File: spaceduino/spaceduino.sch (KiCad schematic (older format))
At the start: 68 parts

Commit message: sntuff
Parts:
- removed Y?: XTAL, symbol Device:Crystal_GND2
- added C17, C18: 22pF, Capacitor_SMD:C_0603_1608Metric, symbol Device:C
- added H1, H2, H3, H4: MountingHole_Pad, MountingHole:MountingHole_2.7mm_Pad, symbol Mechanical:MountingHole_Pad
- added Y1: Crystal, Crystal:Crystal_HC49-U_Vertical, symbol Device:Crystal
- C1, C10, C11, C2, C3, C5, C6, C7, C9: renamed from C?; footprint (none) -> Capacitor_SMD:C_0603_1608Metric
- C12, C15, C16, C4, C8: renamed from C?; footprint (none) -> Capacitor_SMD:C_1206_3216Metric
- C13: renamed from C?; value C -> 1.5nF; footprint (none) -> Capacitor_SMD:C_0603_1608Metric
- C14: renamed from C?; value 100nF -> .1uF; footprint (none) -> Capacitor_SMD:C_0603_1608Metric
- D1, D2: renamed from D?; footprint (none) -> Diode_SMD:D_SOD-123
- D3, D4, D5, D6, D7: renamed from D?; footprint (none) -> LED_SMD:LED_1206_3216Metric
- F1: renamed from F?; footprint (none) -> Fuse:Fuse_1206_3216Metric
- J2: renamed from J?; footprint (none) -> Connector_Card:microSD_HC_Hirose_DM3D-SF
- J3: renamed from J?; footprint (none) -> Connector_PinHeader_2.54mm:PinHeader_2x03_P2.54mm_Vertical
- JCONTAINMENT1: renamed from JCONTAINMENT; footprint (none) -> Connector_PinHeader_2.54mm:PinHeader_1x12_P2.54mm_Vertical
- L1, L2: renamed from L?; footprint (none) -> Inductor_SMD:L_1210_3225Metric
- R1, R10, R11, R12, R13, R14, R15, R16, R17, R18, R19, R2, R20, R21, R22, R23, R24, R25, R26, R27, R3, R4, R5, R6, R7, R8, R9: renamed from R?; footprint (none) -> Resistor_SMD:R_1206_3216Metric
- SW1: renamed from SW?; footprint (none) -> Connector_PinHeader_2.54mm:PinHeader_1x02_P2.54mm_Vertical
- U6: renamed from U?; footprint (none) -> Package_SO:SOIC-8_3.9x4.9mm_P1.27mm
- gave numbers to parts that had none: 8
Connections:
- net +3V3 is gone; now on net +3V0: J2.4 (VDD)
- net I2C_SCL is gone; now on net i2c_scl: JCONTAINMENT1.5 (Pin_5)
- net I2C_SDA is gone; now on net i2c_sda: JCONTAINMENT1.4 (Pin_4)
- net GND: now also C17.2, C18.2, H1.1, H2.1, H3.1, H4.1
- net at U5.7 (XTAL2): now also C18.1, Y1.2
- net at U5.8 (XTAL1): now also C17.1, Y1.1
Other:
- note added: "mounting holes"

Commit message: something
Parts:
- removed C16: C, Capacitor_SMD:C_1206_3216Metric, symbol Device:C
- removed C9: .1uF, Capacitor_SMD:C_0603_1608Metric, symbol Device:C
- removed D2: D, Diode_SMD:D_SOD-123, symbol Device:D
- removed JCONTAINMENT1: Conn_01x12, Connector_PinHeader_2.54mm:PinHeader_1x12_P2.54mm_Vertical, symbol Connector_Generic:Conn_01x12
- removed R11: 5.6k, Resistor_SMD:R_1206_3216Metric, symbol Device:R
- removed R12: 13k, Resistor_SMD:R_1206_3216Metric, symbol Device:R
- removed R13, R16, R18, R26, R27, R9: R, Resistor_SMD:R_1206_3216Metric, symbol Device:R
- removed R14, R15: 1k, Resistor_SMD:R_1206_3216Metric, symbol Device:R
- removed U6: LM358, Package_SO:SOIC-8_3.9x4.9mm_P1.27mm, symbol Amplifier_Operational:LM358
- added C18: 10uF, Capacitor_SMD:C_0603_1608Metric, symbol Device:C
- added D1: D, Diode_SMD:D_SOD-123, symbol Device:D
- added FB1: Ferrite_Bead, Inductor_SMD:L_1206_3216Metric, symbol Device:Ferrite_Bead
- added J?: Conn_02x05_Odd_Even, symbol Connector_Generic:Conn_02x05_Odd_Even
- added LOGO1: Logo_Open_Hardware_Small, Spaceduino:spaceduino-logo, symbol Graphic:Logo_Open_Hardware_Small
- added Q?: PZT3904, Package_TO_SOT_SMD:SOT-223-3_TabPin2, symbol Transistor_BJT:PZT3904
- added R10: 10k, Resistor_SMD:R_1206_3216Metric, symbol Device:R
- added R6: 50m, Resistor_SMD:R_1206_3216Metric, symbol Device:R
- added U5, U7: INA226, Package_SO:VSSOP-10_3x3mm_P0.5mm, symbol Analog_ADC:INA226
- R11: renamed from R10; value .05 -> 50m
- R17: value R -> 10k
- R19, R20: value R -> 470
- R5: value .1 -> 10k
- SW1: footprint Connector_PinHeader_2.54mm:PinHeader_1x02_P2.54mm_Vertical -> Jumper:SolderJumper-2_P1.3mm_Open_TrianglePad1.0x1.5mm
- renumbered C17 to C11, C11 to C12, C18 to C13, C12 to C14, C13 to C15, C14 to C16, C15 to C17, D1 to D2, D4 to D3PWR1, D7 to DALERT1, D5 to DBPWR1, D6 to DIND1, D3 to DPWR1, R3 to R1, R21 to R12, R22 to R13, R23 to R14, R24 to R15, R25 to R16, R4 to R2, R1 to R3, R2 to R4, R6 to R7, R7 to R8, R8 to R9, U5 to U6
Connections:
- net current_trip is gone; now on net +5V: R16.1
- net sd_ss is gone; now on net 4_sd_ss: U3.10 (B4)
- net +5V: now also R17.1, R5.1, D1.1 (K), R10.1, U5.1 (A1), U5.2 (A0), U5.6 (VS), U7.6 (VS), U7.9 (Vin-)
- net 13: no longer R15.1
- net 3: now also R15.1
- net GND: now also C18.2, J?.9 (Pin_9), Q?.3 (E), U5.7 (GND), U7.1 (A1), U7.2 (A0), U7.7 (GND); no longer DALERT1.1 (K), R20.1
- net VDDF: now also R6.1, U5.9 (Vin-); no longer R5.1
- net a7: no longer R17.1
- net i2c_scl: now also J?.3 (Pin_3), U5.5 (SCL), U7.5 (SCL)
- net i2c_sda: now also J?.1 (Pin_1), U5.4 (SDA), U7.4 (SDA)
- net vusb: now also FB1.1; no longer F1.2
- net ~reset: now also R19.2, R5.2, D1.2 (A); no longer SW1.1 (A)
- net d-: now reaches C7.1, J1.2 (D-), R4.2
- net d+: now reaches C6.1, J1.3 (D+), R3.2
- net at Q1.3 (D): now also J?.5 (Pin_5)
- net at Q2.3 (D): now also J?.7 (Pin_7)
- net at C17.1, F1.1, R11.2: now also U7.10 (Vin+), U7.8 (Vbus); no longer R19.2
- net at C14.1, C15.1, D2.1 (K)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: now also R6.2, U5.10 (Vin+), U5.8 (Vbus); no longer R5.2
- net at R17.2: now also R20.1, C18.1, Q?.1 (B)
- net at R19.1: now also SW1.1 (A); no longer R20.2
- net at Q1.1 (G), Q2.1 (G): now also Q?.2 (C), Q?.4 (C), R10.2
- net 4 renamed 4_sd_ss
- new net: F1.2, FB1.2
- new net current_trip_fast: DALERT1.1 (K), R20.2, U7.3 (~Alert~)
- no-connect marks 9 -> 10
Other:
- note added: "<- can be LED"
- note added: "current limiting"
- note removed: "TODO: sense"
- note removed: "Voltage Monitoring"
- note removed: "circular connector"
- note removed: "increase ratio for\nlarge boost voltage"
- moved on the sheet: D3PWR1, DALERT1, DBPWR1, DIND1, DPWR1, H1, H2, H3, H4, Q1, Q2, R12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

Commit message: spaceduino simple finished
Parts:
- removed Q?: PZT3904, Package_TO_SOT_SMD:SOT-223-3_TabPin2, symbol Transistor_BJT:PZT3904
- added C19, C9: .1uF, Capacitor_SMD:C_0603_1608Metric, symbol Device:C
- added Q3: 2N7002, Package_TO_SOT_SMD:SOT-23, symbol Transistor_FET:2N7002
- added R18: 3.3k, Resistor_SMD:R_1206_3216Metric, symbol Device:R
- H1, H2, H3, H4: footprint MountingHole:MountingHole_2.7mm_Pad -> MountingHole:MountingHole_2.2mm_M2_Pad
- J4: renamed from J?; footprint (none) -> Connector_PinHeader_2.54mm:PinHeader_2x05_P2.54mm_Vertical
- R10: value 10k -> 36k
- R17: value 10k -> 3.3k
- renumbered J2 to MICROSD1
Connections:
- net labels added: 2_boost_en, current_trip
- net labels removed: 2, boost_en, current_trip_fast
- wire segments 165 -> 174
- no-connect marks 10 -> 15
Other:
- moved on the sheet: C18, R10, R20

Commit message: spaceduino Rev. 1
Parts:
- removed Q3: 2N7002, Package_TO_SOT_SMD:SOT-23, symbol Transistor_FET:2N7002
- added Q3: BSS84, Package_TO_SOT_SMD:SOT-23, symbol Transistor_FET:BSS84
- L2: value L -> 10uH
- R19, R20: value 470 -> 100
- R8: value 13k -> 10k
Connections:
- wire segments 174 -> 176
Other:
- moved on the sheet: C18, R10, R20
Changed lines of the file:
@@
 $Descr A4 11693 8268
 encoding utf-8
-Sheet 1 1
+Sheet 1 2
 Title "Spaceduino"
 Date ""
@@
 P 1400 3300
 F 0 "L2" V 1219 3300 50  0000 C CNN
-F 1 "L" V 1310 3300 50  0000 C CNN
+F 1 "10uH" V 1310 3300 50  0000 C CNN
 F 2 "Inductor_SMD:L_1210_3225Metric" H 1400 3300 50  0001 C CNN
 F 3 "~" H 1400 3300 50  0001 C CNN
@@
 	1    0    0    -1
 $EndComp
-$Comp
-L Device:R R8
-U 1 1 5F23B068
-P 850 4000
-F 0 "R8" H 780 3954 50  0000 R CNN
-F 1 "13k" H 780 4045 50  0000 R CNN
-F 2 "Resistor_SMD:R_1206_3216Metric" V 780 4000 50  0001 C CNN
-F 3 "~" H 850 4000 50  0001 C CNN
-	1    850  4000
-	-1   0    0    1
-$EndComp
-Connection ~ 850  3850
-Wire Wire Line
-	1100 4050 1100 4150
-Wire Wire Line
-	1100 4150 850  4150
-Text GLabel 1000 4150 3    50   Input ~ 0
+Text GLabel 1100 4050 0    50   Input ~ 0
 2_boost_en
 $Comp
@@
 	8250 5800 8250 5400
 Connection ~ 8250 5800
-Text GLabel 2500 5900 2    50   Input ~ 0
+Text GLabel 2200 5100 1    50   Input ~ 0
 current_trip
-Wire Wire Line
-	9850 4650 9450 4650
 $Comp
 L Analog_ADC:INA226 U5
@@
 L Device:R R10
 U 1 1 5F2E7DDA
-P 9450 4500
-F 0 "R10" H 9520 4546 50  0000 L CNN
-F 1 "36k" H 9520 4455 50  0000 L CNN
-F 2 "Resistor_SMD:R_1206_3216Metric" V 9380 4500 50  0001 C CNN
-F 3 "~" H 9450 4500 50  0001 C CNN
-	1    9450 4500
-	1    0    0    -1
-$EndComp
-$Comp
-L power:+5V #PWR036
-U 1 1 5F2E8D07
-P 9450 4350
-F 0 "#PWR036" H 9450 4200 50  0001 C CNN
-F 1 "+5V" H 9465 4523 50  0000 C CNN
-F 2 "" H 9450 4350 50  0001 C CNN
-F 3 "" H 9450 4350 50  0001 C CNN
-	1    9450 4350
-	1    0    0    -1
-$EndComp
-$Comp
-L power:+5V #PWR043
-U 1 1 5F2E9BF9
-P 2200 5100
-F 0 "#PWR043" H 2200 4950 50  0001 C CNN
-F 1 "+5V" H 2215 5273 50  0000 C CNN
-F 2 "" H 2200 5100 50  0001 C CNN
-F 3 "" H 2200 5100 50  0001 C CNN
-	1    2200 5100
+P 10550 6050
+F 0 "R10" H 10620 6096 50  0000 L CNN
+F 1 "36k" H 10620 6005 50  0000 L CNN
+F 2 "Resistor_SMD:R_1206_3216Metric" V 10480 6050 50  0001 C CNN
+F 3 "~" H 10550 6050 50  0001 C CNN
+	1    10550 6050
 	1    0    0    -1
 $EndComp
@@
 P 3200 6450
 F 0 "R19" V 2993 6450 50  0000 C CNN
-F 1 "470" V 3084 6450 50  0000 C CNN
+F 1 "100" V 3084 6450 50  0000 C CNN
 F 2 "Resistor_SMD:R_1206_3216Metric" V 3130 6450 50  0001 C CNN
 F 3 "~" H 3200 6450 50  0001 C CNN
@@
 Text Notes 4850 2950 0    39   ~ 0
 <- can be LED
-$Comp
-L Device:R R20
-U 1 1 5F18D89A
-P 9450 6000
-F 0 "R20" H 9520 6046 50  0000 L CNN
-F 1 "470" H 9520 5955 50  0000 L CNN
-F 2 "Resistor_SMD:R_1206_3216Metric" V 9380 6000 50  0001 C CNN
-F 3 "~" H 9450 6000 50  0001 C CNN
-	1    9450 6000
-	0    1    1    0
-$EndComp
 $Comp
 L Device:Ferrite_Bead FB1
@@
 	1    0    0    -1
 $EndComp
-Wire Wire Line
-	8800 4650 8800 4300
 Connection ~ 8800 4300
 Text GLabel 1800 5100 1    50   Input ~ 0
@@
 	1    0    0    -1
 $EndComp
-Wire Wire Line
-	9050 6000 9300 6000
 $Comp
 L power:PWR_FLAG #FLG0101
@@
 L power:GND #PWR056
 U 1 1 5F213441
-P 9850 6300
-F 0 "#PWR056" H 9850 6050 50  0001 C CNN
-F 1 "GND" H 9855 6127 50  0000 C CNN
-F 2 "" H 9850 6300 50  0001 C CNN
-F 3 "" H 9850 6300 50  0001 C CNN
-	1    9850 6300
+P 10150 6200
+F 0 "#PWR056" H 10150 5950 50  0001 C CNN
+F 1 "GND" H 10155 6027 50  0000 C CNN
+F 2 "" H 10150 6200 50  0001 C CNN
+F 3 "" H 10150 6200 50  0001 C CNN
+	1    10150 6200
 	1    0    0    -1
 $EndComp
@@
 L Device:C C18
 U 1 1 5F203B58
-P 9850 6150
-F 0 "C18" H 9965 6196 50  0000 L CNN
-F 1 "10uF" H 9965 6105 50  0000 L CNN
-F 2 "Capacitor_SMD:C_0603_1608Metric" H 9888 6000 50  0001 C CNN
-F 3 "~" H 9850 6150 50  0001 C CNN
-	1    9850 6150
-	1    0    0    -1
-$EndComp
-Wire Wire Line
-	9850 4650 9850 6000
-Text GLabel 9850 4950 0    50   Input ~ 0
+P 10150 6050
+F 0 "C18" H 10265 6096 50  0000 L CNN
+F 1 "10uF" H 10265 6005 50  0000 L CNN
+F 2 "Capacitor_SMD:C_0603_1608Metric" H 10188 5900 50  0001 C CNN
+F 3 "~" H 10150 6050 50  0001 C CNN
+	1    10150 6050
+	1    0    0    -1
+$EndComp
+Text GLabel 10550 5550 2    50   Input ~ 0
 current_trip
 $Comp
 L power:GND #PWR0105
 U 1 1 5F2F2AE3
-P 2200 6100
-F 0 "#PWR0105" H 2200 5850 50  0001 C CNN
-F 1 "GND" H 2205 5927 50  0000 C CNN
-F 2 "" H 2200 6100 50  0001 C CNN
-F 3 "" H 2200 6100 50  0001 C CNN
-	1    2200 6100
-	1    0    0    -1
-$EndComp
-Connection ~ 9850 6000
-Wire Wire Line
-	9850 6000 9600 6000
-Connection ~ 9450 4650
-Wire Wire Line
-	9450 4650 8800 4650
-$Comp
-L Transistor_FET:2N7002 Q3
-U 1 1 5F32572F
-P 2300 5900
-F 0 "Q3" H 2505 5946 50  0000 L CNN
-F 1 "2N7002" H 2505 5855 50  0000 L CNN
-F 2 "Package_TO_SOT_SMD:SOT-23" H 2500 5825 50  0001 L CIN
-F 3 "https://www.fairchildsemi.com/datasheets/2N/2N7002.pdf" H 2300 5900 50  0001 L CNN
-	1    2300 5900
-	-1   0    0    -1
+P 2200 5700
+F 0 "#PWR0105" H 2200 5450 50  0001 C CNN
+F 1 "GND" H 2205 5527 50  0000 C CNN
+F 2 "" H 2200 5700 50  0001 C CNN
+F 3 "" H 2200 5700 50  0001 C CNN
+	1    2200 5700
+	1    0    0    -1
 $EndComp
 Wire Wire Line
@@
 	1    0    0    -1
 $EndComp
+$Sheet
+S 2000 6950 1150 550
+U 5F218DF1
+F0 "Custom" 50
+F1 "custom.sch" 50
+$EndSheet
+$Comp
+L Transistor_FET:BSS84 Q3
+U 1 1 5F22DFC7
+P 10050 5150
+F 0 "Q3" H 10254 5196 50  0000 L CNN
+F 1 "BSS84" H 10254 5105 50  0000 L CNN
+F 2 "Package_TO_SOT_SMD:SOT-23" H 10250 5075 50  0001 L CIN
+F 3 "http://assets.nexperia.com/documents/data-sheet/BSS84.pdf" H 10050 5150 50  0001 L CNN
+	1    10050 5150
+	1    0    0    -1
+$EndComp
+Wire Wire Line
+	10150 5700 10150 5800
+Wire Wire Line
+	9850 6000 9850 5150
+Wire Wire Line
+	10150 5800 10550 5800
+Connection ~ 10150 5800
+Wire Wire Line
+	10150 5800 10150 5900
+$Comp
+L power:GND #PWR0106
+U 1 1 5F2C0CAC
+P 10550 6200
+F 0 "#PWR0106" H 10550 5950 50  0001 C CNN
+F 1 "GND" H 10555 6027 50  0000 C CNN
+F 2 "" H 10550 6200 50  0001 C CNN
+F 3 "" H 10550 6200 50  0001 C CNN
+	1    10550 6200
+	1    0    0    -1
+$EndComp
+Wire Wire Line
+	10550 5900 10550 5800
+Wire Wire Line
+	10550 5800 10550 4300
+Wire Wire Line
+	8800 4300 10550 4300
+Connection ~ 10550 5800
+$Comp
+L power:+5V #PWR0107
+U 1 1 5F2D4A45
+P 10150 4950
+F 0 "#PWR0107" H 10150 4800 50  0001 C CNN
+F 1 "+5V" H 10165 5123 50  0000 C CNN
+F 2 "" H 10150 4950 50  0001 C CNN
+F 3 "" H 10150 4950 50  0001 C CNN
+	1    10150 4950
+	1    0    0    -1
+$EndComp
+$Comp
+L Device:R R20
+U 1 1 5F18D89A
+P 10150 5550
+F 0 "R20" H 10220 5596 50  0000 L CNN
+F 1 "100" H 10220 5505 50  0000 L CNN
+F 2 "Resistor_SMD:R_1206_3216Metric" V 10080 5550 50  0001 C CNN
+F 3 "~" H 10150 5550 50  0001 C CNN
+	1    10150 5550
+	-1   0    0    1
+$EndComp
+Wire Wire Line
+	10150 5400 10150 5350
+Wire Wire Line
+	9050 6000 9850 6000
+$Comp
+L Device:R R8
+U 1 1 5F31F32C
+P 9850 4900
+F 0 "R8" H 9920 4946 50  0000 L CNN
+F 1 "10k" H 9920 4855 50  0000 L CNN
+F 2 "Resistor_SMD:R_1206_3216Metric" V 9780 4900 50  0001 C CNN
+F 3 "~" H 9850 4900 50  0001 C CNN
+	1    9850 4900
+	1    0    0    -1
+$EndComp
+Wire Wire Line
+	9850 5050 9850 5150
+Connection ~ 9850 5150
+$Comp
+L power:+5V #PWR0108
+U 1 1 5F3293B7
+P 9850 4750
+F 0 "#PWR0108" H 9850 4600 50  0001 C CNN
+F 1 "+5V" H 9865 4923 50  0000 C CNN
+F 2 "" H 9850 4750 50  0001 C CNN
+F 3 "" H 9850 4750 50  0001 C CNN
+	1    9850 4750
+	1    0    0    -1
+$EndComp

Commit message: jk, /this/ is the spaceduino 1.0! (actually, just look at git tags)
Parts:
- added C20: .1uF, Capacitor_SMD:C_0603_1608Metric, symbol Device:C
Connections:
- net +3V0: now also C20.1
- net GND: now also C20.2
- net spi_miso renamed 6_spi_miso
- net spi_mosi renamed 5_spi_mosi
- net spi_sck renamed 7_spi_sck
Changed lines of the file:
@@
 $EndComp
 Text GLabel 6800 1350 0    50   Input ~ 0
-spi_miso
+6_spi_miso
 Text GLabel 6800 1550 0    50   Input ~ 0
-spi_sck
+7_spi_sck
 Text GLabel 6800 1750 0    50   Input ~ 0
-spi_mosi
+5_spi_mosi
 Text GLabel 6800 1950 0    50   Input ~ 0
 4_sd_ss
@@
 i2c_scl
 Text GLabel 4750 5750 2    39   Input ~ 0
-spi_mosi
+5_spi_mosi
 Text GLabel 4250 5650 0    39   Input ~ 0
-spi_miso
+6_spi_miso
 Text GLabel 4250 5750 0    39   Input ~ 0
-spi_sck
+7_spi_sck
 Text GLabel 4250 5850 0    39   Input ~ 0
 ~reset
 Text GLabel 6300 4550 2    39   Input ~ 0
-spi_mosi
+5_spi_mosi
 Text GLabel 6300 4650 2    39   Input ~ 0
-spi_miso
+6_spi_miso
 Text GLabel 6300 4750 2    39   Input ~ 0
-spi_sck
+7_spi_sck
 Wire Wire Line
 	7650 950  7300 950
@@
 	1    0    0    -1
 $EndComp
+$Comp
+L power:+3V0 #PWR0109
+U 1 1 5F37D0F6
+P 6650 700
+F 0 "#PWR0109" H 6650 550 50  0001 C CNN
+F 1 "+3V0" H 6665 873 50  0000 C CNN
+F 2 "" H 6650 700 50  0001 C CNN
+F 3 "" H 6650 700 50  0001 C CNN
+	1    6650 700
+	1    0    0    -1
+$EndComp
+$Comp
+L Device:C C20
+U 1 1 5F37E1E3
+P 6650 850
+F 0 "C20" H 6765 896 50  0000 L CNN
+F 1 ".1uF" H 6765 805 50  0000 L CNN
+F 2 "Capacitor_SMD:C_0603_1608Metric" H 6688 700 50  0001 C CNN
+F 3 "~" H 6650 850 50  0001 C CNN
+	1    6650 850
+	1    0    0    -1
+$EndComp
+$Comp
+L power:GND #PWR0110
+U 1 1 5F392DCB
+P 6650 1000
+F 0 "#PWR0110" H 6650 750 50  0001 C CNN
+F 1 "GND" H 6655 827 50  0000 C CNN
+F 2 "" H 6650 1000 50  0001 C CNN
+F 3 "" H 6650 1000 50  0001 C CNN
+	1    6650 1000
+	1    0    0    -1
+$EndComp

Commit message: ok, flipped a mosfet, NOW im done
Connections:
- net +5V: now also Q3.2 (S); no longer Q3.3 (D)
- net at R20.2: now also Q3.3 (D); no longer Q3.2 (S)
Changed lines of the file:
@@
 Text GLabel 9550 3650 0    39   Input ~ 0
 i2c_scl
-Text GLabel 4750 5750 2    39   Input ~ 0
-5_spi_mosi
 Text GLabel 4250 5650 0    39   Input ~ 0
 6_spi_miso
@@
 F 3 "http://assets.nexperia.com/documents/data-sheet/BSS84.pdf" H 10050 5150 50  0001 L CNN
 	1    10050 5150
-	1    0    0    -1
+	1    0    0    1
 $EndComp
 Wire Wire Line
@@
 	1    0    0    -1
 $EndComp
+Text GLabel 4750 5750 2    39   Input ~ 0
+5_spi_mosi
 $EndSCHEMATC

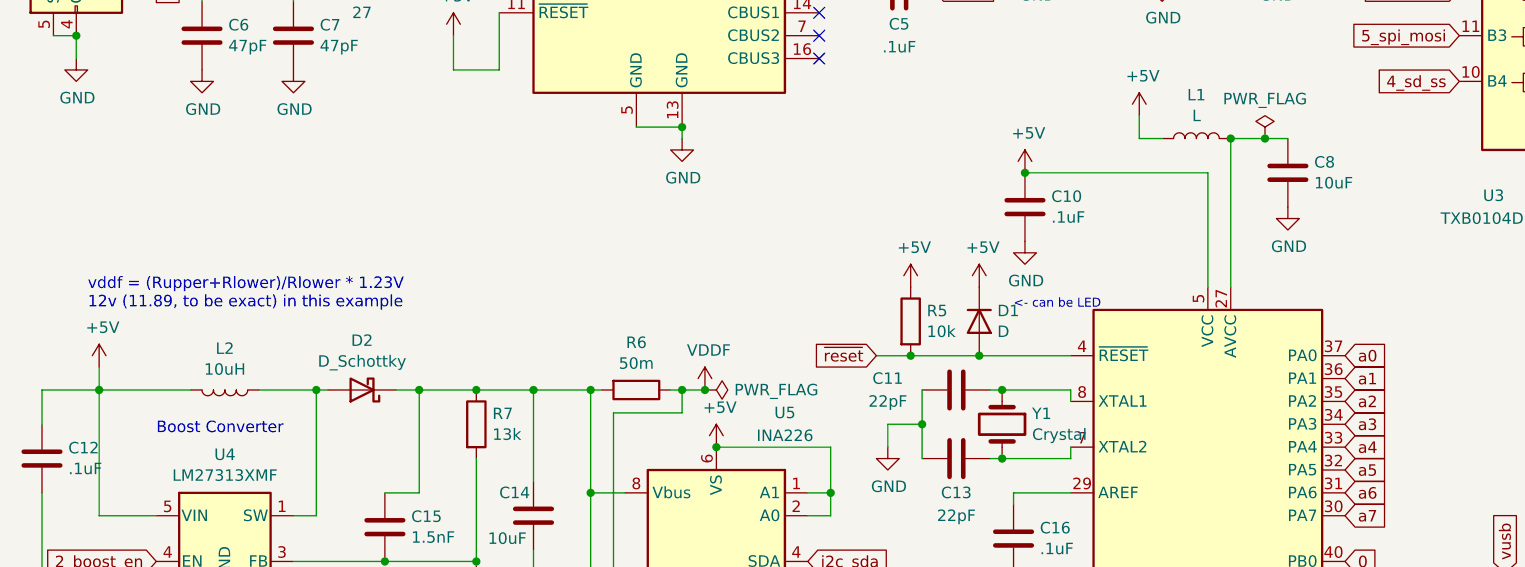
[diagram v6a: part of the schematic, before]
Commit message: add an extra inductor for the boost converter
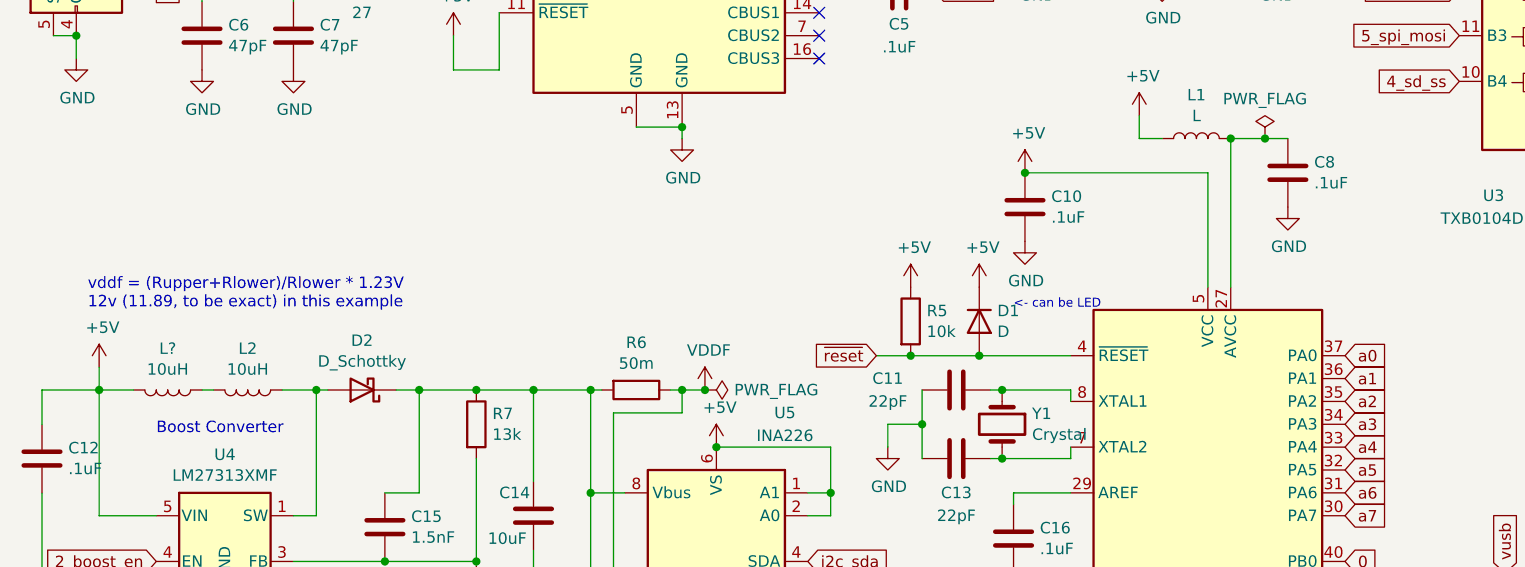
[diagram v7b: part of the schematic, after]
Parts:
- added L?: 10uH, Inductor_SMD:L_1210_3225Metric, symbol Device:L
- C8: value 10uF -> .1uF
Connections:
- net +5V: now also L?.2; no longer L2.2
- new net: L2.2, L?.1
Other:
- moved on the sheet: L2
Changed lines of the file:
@@
 	6050 2200 5950 2200
-$Comp
-L Device:C C8
-U 1 1 5EFBEB67
-P 6050 2350
-F 0 "C8" H 6165 2396 50  0000 L CNN
-F 1 "10uF" H 6165 2305 50  0000 L CNN
-F 2 "Capacitor_SMD:C_1206_3216Metric" H 6088 2200 50  0001 C CNN
-F 3 "~" H 6050 2350 50  0001 C CNN
-	1    6050 2350
-	1    0    0    -1
-$EndComp
 $Comp
 L power:GND #PWR022
@@
 L Device:L L2
 U 1 1 5F0C1462
-P 1400 3300
-F 0 "L2" V 1219 3300 50  0000 C CNN
-F 1 "10uH" V 1310 3300 50  0000 C CNN
-F 2 "Inductor_SMD:L_1210_3225Metric" H 1400 3300 50  0001 C CNN
-F 3 "~" H 1400 3300 50  0001 C CNN
-	1    1400 3300
+P 1500 3300
+F 0 "L2" V 1319 3300 50  0000 C CNN
+F 1 "10uH" V 1410 3300 50  0000 C CNN
+F 2 "Inductor_SMD:L_1210_3225Metric" H 1500 3300 50  0001 C CNN
+F 3 "~" H 1500 3300 50  0001 C CNN
+	1    1500 3300
 	0    1    1    0
 $EndComp
@@
 $EndComp
 Wire Wire Line
-	1550 3300 1800 3300
+	1650 3300 1800 3300
 Wire Wire Line
 	1700 3850 1800 3850
@@
 	1    0    0    -1
 $EndComp
-Wire Wire Line
-	850  3300 1250 3300
 Wire Wire Line
 	1100 3850 850  3850
@@
 Text GLabel 4750 5750 2    39   Input ~ 0
 5_spi_mosi
+$Comp
+L Device:C C8
+U 1 1 5EFBEB67
+P 6050 2350
+F 0 "C8" H 6165 2396 50  0000 L CNN
+F 1 ".1uF" H 6165 2305 50  0000 L CNN
+F 2 "Capacitor_SMD:C_1206_3216Metric" H 6088 2200 50  0001 C CNN
+F 3 "~" H 6050 2350 50  0001 C CNN
+	1    6050 2350
+	1    0    0    -1
+$EndComp
+$Comp
+L Device:L L?
+U 1 1 5F494F30
+P 1150 3300
+F 0 "L?" V 969 3300 50  0000 C CNN
+F 1 "10uH" V 1060 3300 50  0000 C CNN
+F 2 "Inductor_SMD:L_1210_3225Metric" H 1150 3300 50  0001 C CNN
+F 3 "~" H 1150 3300 50  0001 C CNN
+	1    1150 3300
+	0    1    1    0
+$EndComp
+Wire Wire Line
+	1300 3300 1350 3300
+Wire Wire Line
+	1000 3300 850  3300
 $EndSCHEMATC
